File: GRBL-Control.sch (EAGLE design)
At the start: 55 parts, among them IC3 4050D, IC4 LP298XS, J1 MICRO SD, SW1 B3U-1000PM-B, SW2 B3U-1000PM-B, SW3 B3U-1000PM-B, SW4 B3U-1000PM-B, U1 ARDUINO, U2 ARDUINO MICRO, U3 LM2596, X1 MSTBA2, X2 MSTBA8, X3 MSTBA12

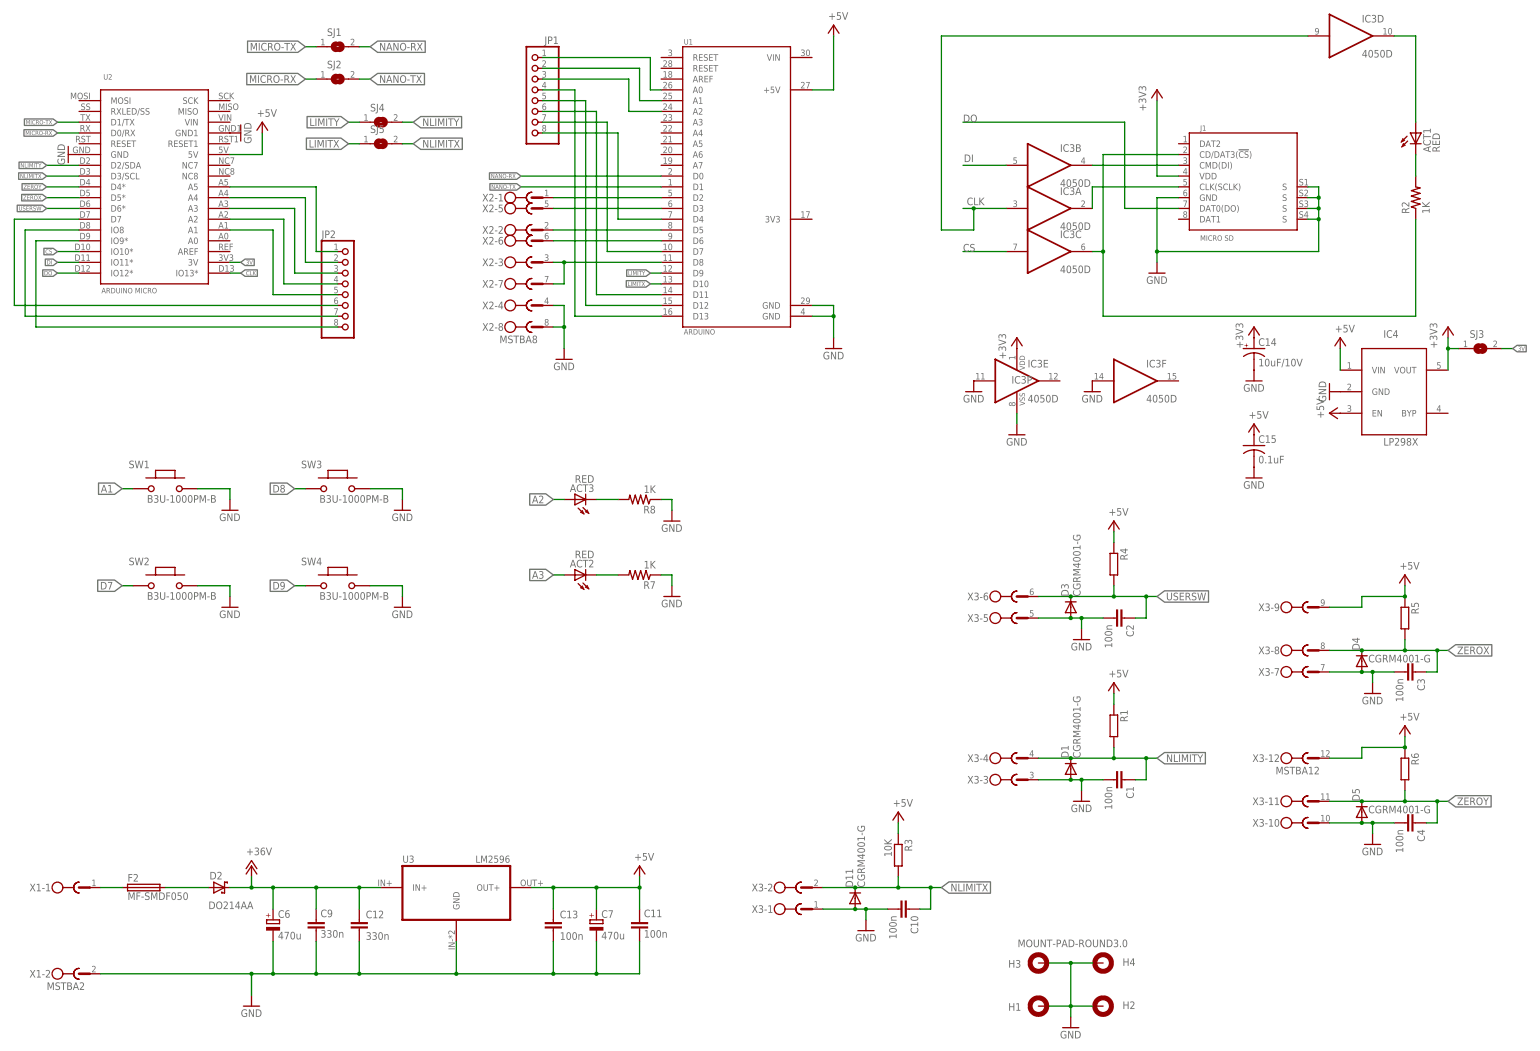
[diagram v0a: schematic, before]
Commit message: v1.1 changed level converter for SD card, added soldering place and some other minor changes
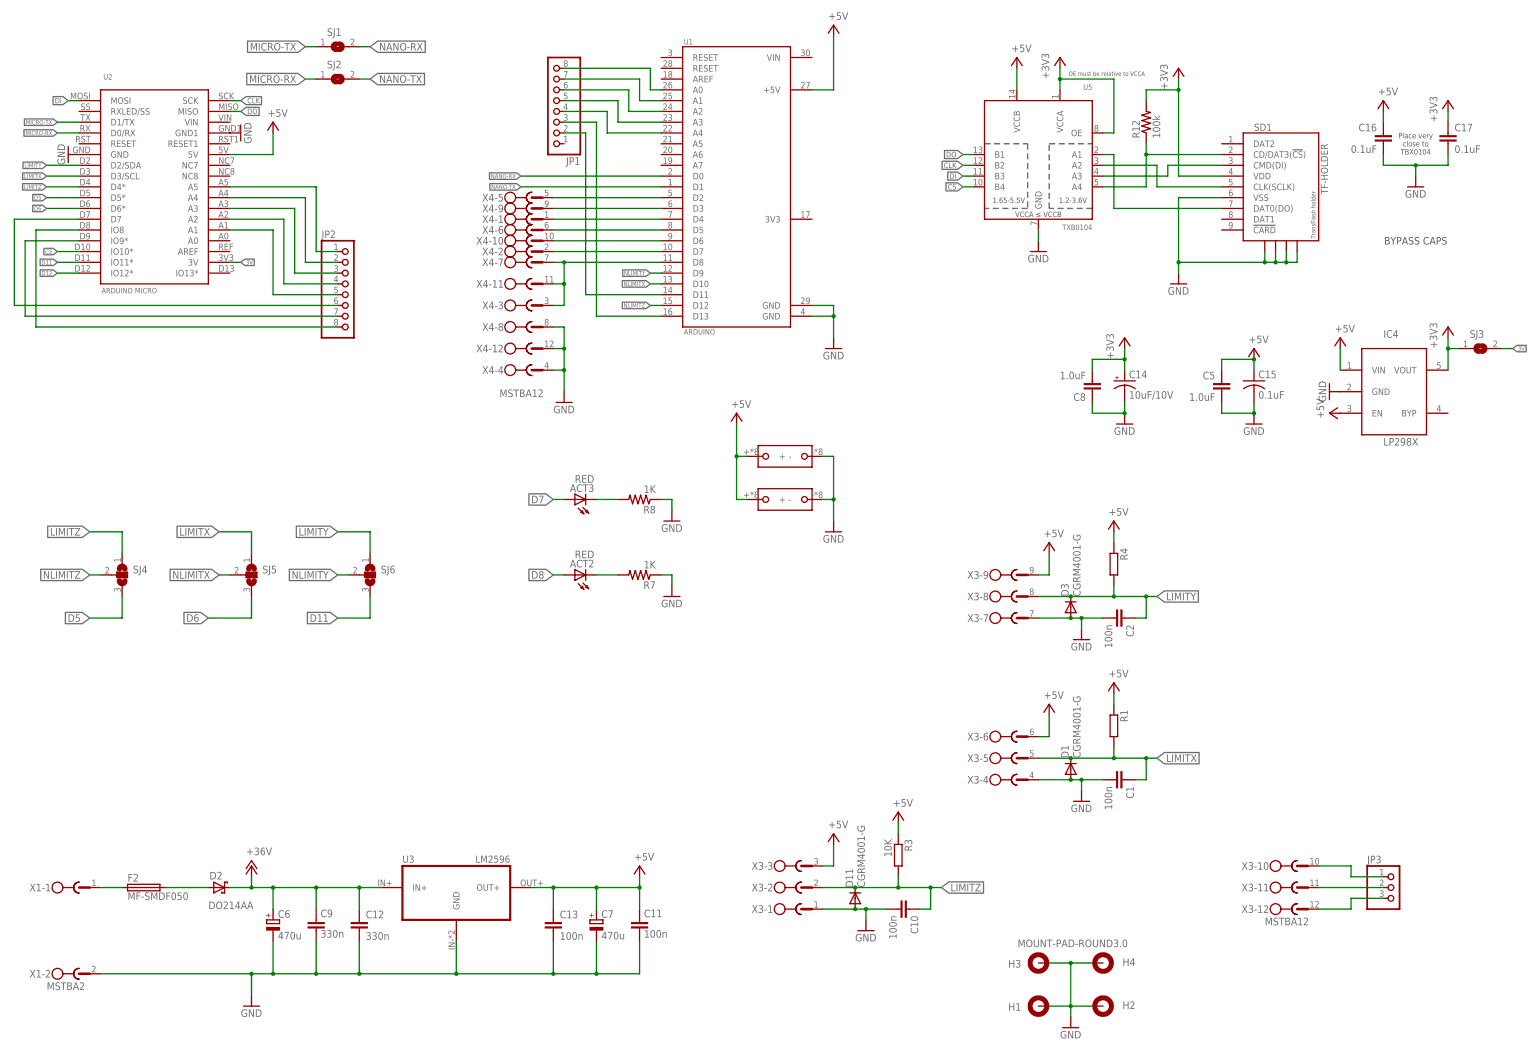
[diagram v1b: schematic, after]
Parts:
- removed ACT1: RED, adafruit:LEDCHIP-LED0805
- removed C3, C4: 100n, Parts:C-EUC0603
- removed D4, D5: CGRM4001-G, Parts:CGRM4001-G
- removed IC3: 4050D, 40xx:4050D
- removed J1: MICRO SD, sd-mmc:TRANSFLASH-LOCK
- removed R2: 1K, adafruit:R-US_R0805
- removed R5, R6: (no value), Parts:R-EU_R0603
- removed SW1, SW2, SW3, SW4: B3U-1000PM-B, Parts:MYSMD_PB157B3U
- removed X2: MSTBA8, Parts:MSTBA8
- added C16, C17: 0.1uF, SparkFun-Capacitors:0.1UF-25V(+80/-20%)(0603)
- added C5, C8: 1.0uF, SparkFun-Capacitors:1.0UF-16V-10%(0603)
- added JP3: (no value), pinhead:PINHD-1X3
- added R12: 100k, SparkFun-Resistors:100KOHM-1/10W-1%(0603)
- added SD1: TF-HOLDER, sd-mmc:TF-HOLDER
- added SJ6: (no value), jumper:SJ2W
- added U$1, U$2: DEV_GRID, Components:DEV_GRID
- added U5: TXB0104, SparkFun-DigitalIC:TXB0104PWRSOIC14
- added X4: MSTBA12, con-phoenix-508:MSTBA12
- SJ4, SJ5: device jumper:SJ -> jumper:SJ2W
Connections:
- removed net NA0: JP1.1, U1.A0
- removed net NA1: JP1.2, U1.A1
- removed net NA2: JP1.3, U1.A2
- removed net ND11: JP1.6, U1.D11
- removed net ND12: JP1.5, U1.D12
- removed net ND13: JP1.4, U1.D13
- removed net ND4: JP1.8, U1.D4
- removed net ND7: JP1.7, U1.D7
- removed net USERSW: C2.1, D3.C, R4.2, U2.D6*, X3-6.1
- removed net ZEROX: C3.1, D4.C, R5.2, U2.D5*, X3-8.1
- removed net ZEROY: C4.1, D5.C, R6.2, U2.D4*, X3-11.1
- new net !CS_3V3: R12.1, SD1.CD/DAT3(!CS!), U5.A4
- new net CLK_3V3: SD1.CLK(SCLK), U5.A2
- new net D11: SJ6.3, U2.IO11*
- new net D12: U2.IO12*
- new net D5: SJ4.3, U2.D5*
- new net D6: SJ5.3, U2.D6*
- new net DI_3V3: SD1.CMD(DI), U5.A3
- new net DO_3V3: SD1.DAT0(DO), U5.A1
- new net LIMITZ: C10.1, D11.C, R3.2, SJ4.1, U2.D4*, X3-2.1
- new net N$14: JP3.2, X3-11.1
- new net N$15: JP3.3, X3-12.1
- new net N$4: U1.D4, X4-1.1
- new net N$5: U1.D7, X4-2.1
- new net N$6: JP1.8, U1.A0
- new net N$7: JP1.7, U1.A1
- new net N$8: JP1.6, U1.A2
- new net NLIMITZ: SJ4.2, U1.D12
- net +3V3: now also C17.1, C8.2, R12.2, SD1.VDD, U5.OE, U5.VCCA; no longer IC3P.VDD, J1.VDD
- net +5V: now also C16.1, C5.1, U$1.+, U$2.+, U5.VCCB, X3-3.1, X3-6.1; no longer R5.1, R6.1, X3-12.1
- net A1: no longer SW1.1
- net A2: no longer ACT3.A
- net A3: no longer ACT2.A
- net CLK: now also U2.SCK, U5.B2; no longer IC3A.I, IC3D.I, U2.IO13*
- net CS: now also U5.B4; no longer IC3C.I
- net D7: now also ACT3.A; no longer SW2.1
- net D8: now also ACT2.A, JP2.8; no longer JP2.7, SW3.1
- net D9: now also JP2.7; no longer JP2.8, SW4.1
- net DI: now also U2.MOSI, U5.B3; no longer IC3B.I, U2.IO11*
- net DIRX: now also X4-6.1; no longer X2-2.1
- net DIRY: now also X4-10.1; no longer X2-6.1
- net DO: now also U2.MISO, U5.B1; no longer J1.DAT0(DO), U2.IO12*
- net GND: now also C16.2, C17.2, C5.2, C8.1, SD1.S1, SD1.S2, SD1.S3, SD1.S4, SD1.VSS, U$1.-, U$2.-, U5.GND, X3-4.1, X4-12.1, X4-4.1, X4-8.1; no longer C3.2, C4.2, D4.A, D5.A, IC3E.I, IC3F.I, IC3P.VSS, J1.GND, J1.S@1, J1.S@2, J1.S@3, J1.S@4, SW1.2, SW2.2, SW3.2, SW4.2, X2-4.1, X2-8.1, X3-10.1, X3-3.1, X3-5.1
- net LIMITX: now also C1.1, D1.C, R1.2, U2.D3/SCL, X3-5.1; no longer U1.D10
- net LIMITY: now also C2.1, D3.C, R4.2, SJ6.1, U2.D2/SDA, X3-8.1; no longer SJ4.1, U1.D9
- net N$10: now also JP1.4, U1.A4; no longer IC3A.O, J1.CLK(SCLK)
- net N$11: now also JP1.3, U1.D13; no longer IC3C.O, J1.CD/DAT3(!CS!), R2.1
- net N$12: now also JP1.2, U1.D11; no longer ACT1.C, R2.2
- net N$13: now also JP3.1, X3-10.1; no longer IC3B.O, J1.CMD(DI)
- net N$9: now also JP1.5, U1.A3; no longer ACT1.A, IC3D.O
- net NLIMITX: now also U1.D10; no longer C10.1, D11.C, R3.2, U2.D3/SCL, X3-2.1
- net NLIMITY: now also SJ6.2, U1.D9; no longer C1.1, D1.C, R1.2, SJ4.2, U2.D2/SDA, X3-4.1
- net STEP-EN: now also X4-11.1, X4-3.1, X4-7.1; no longer X2-3.1, X2-7.1
- net STEPX: now also X4-5.1; no longer X2-1.1
- net STEPY: now also X4-9.1; no longer X2-5.1
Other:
- note added: "BYPASS CAPS"
- note added: "OE must be relative to VCCA"
- note added: "Place very close to TBX0104"
- moved on the sheet: C14, C15, JP1, X3-10, X3-11, X3-12, X3-3, X3-4, X3-5, X3-6, X3-7, X3-8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
